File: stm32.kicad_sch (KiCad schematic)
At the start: 13 parts, among them J102 Conn_ARM_JTAG_SWD_10, U101 STM32F302CBTx, Y101 8MHz / 20pF

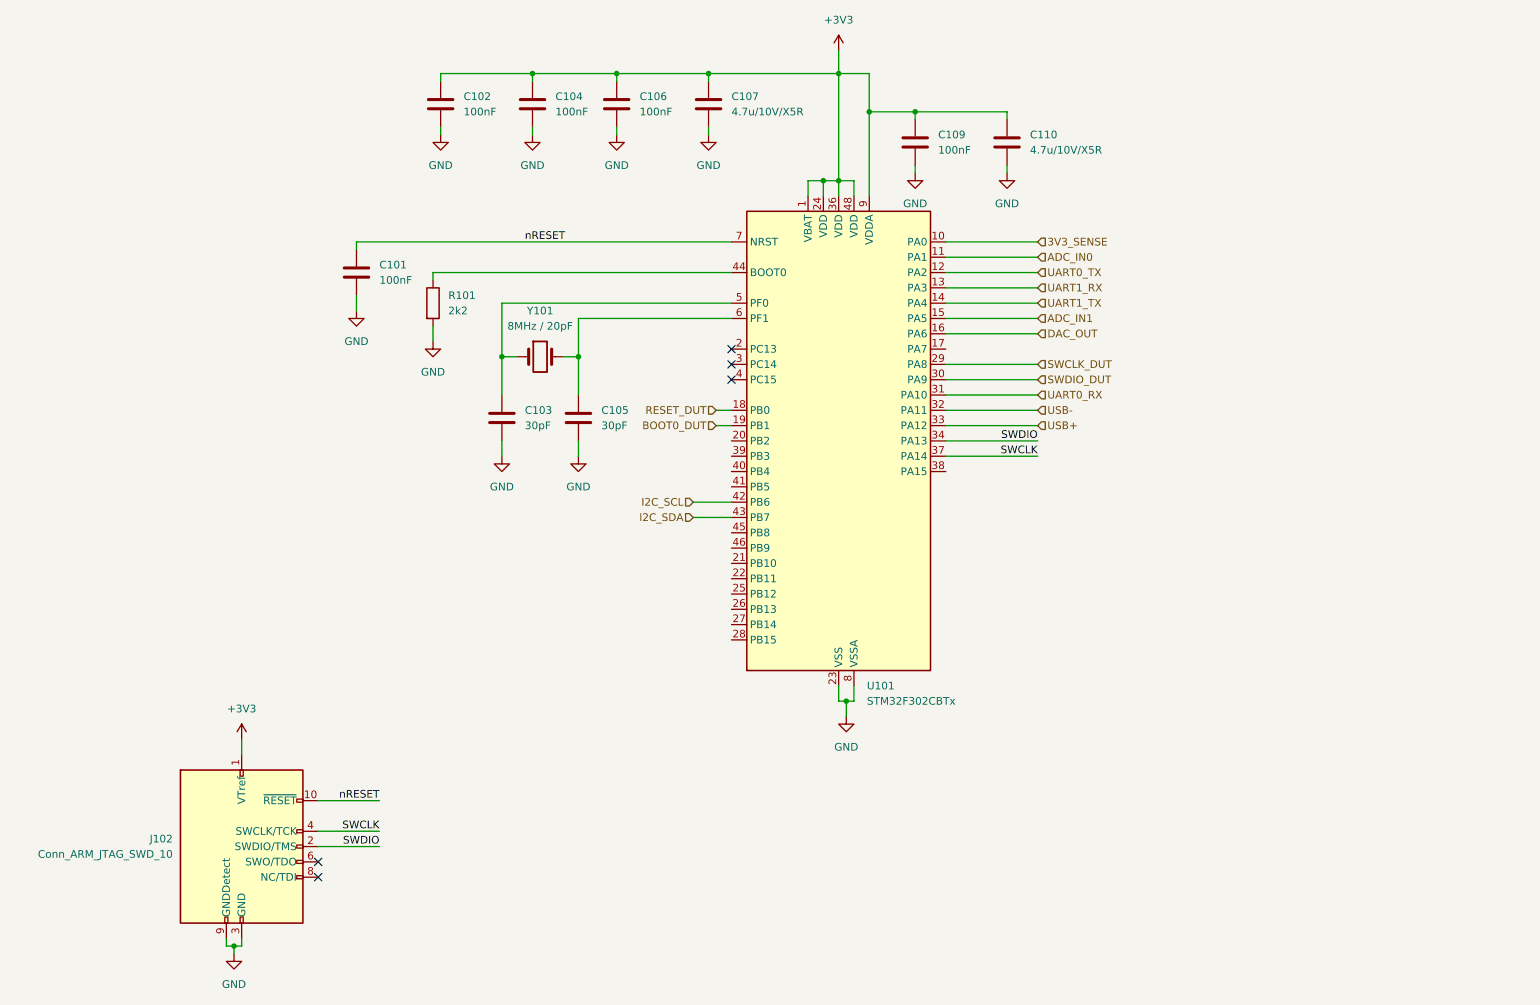
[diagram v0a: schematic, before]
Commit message: add basic structure, update readme
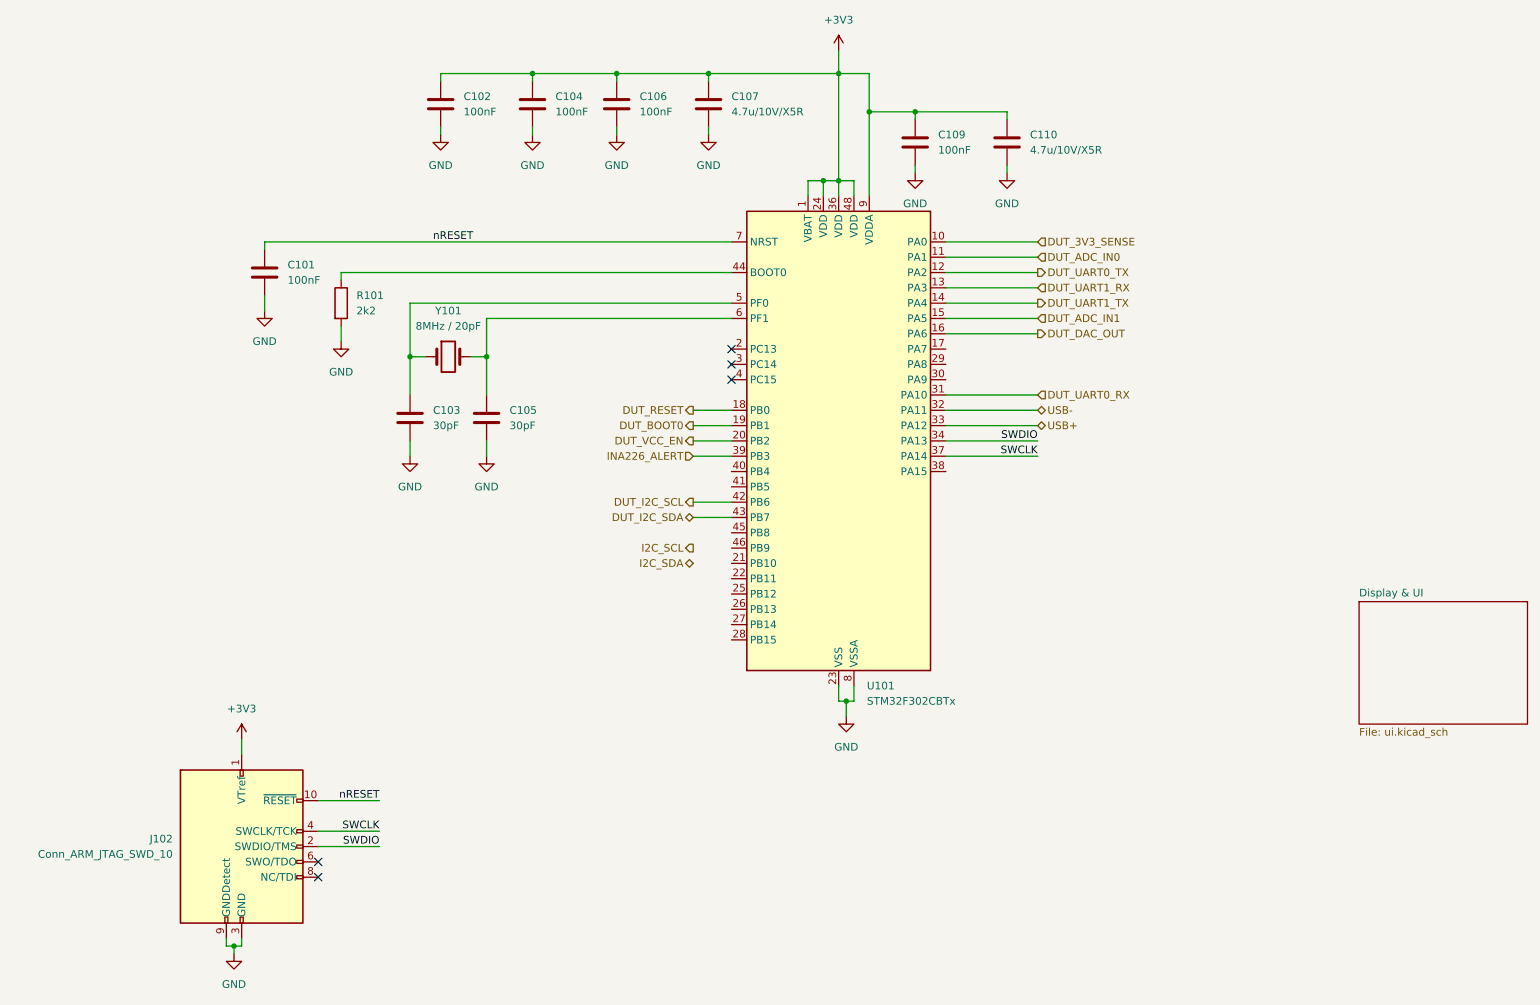
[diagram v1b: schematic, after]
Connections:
- net I2C_SCL: no longer U101.42 (PB6)
- net I2C_SDA: no longer U101.43 (PB7)
- net DUT_VCC_EN: now reaches U101.20 (PB2)
- net INA226_ALERT: now reaches U101.39 (PB3)
- net 3V3_SENSE renamed DUT_3V3_SENSE
- net ADC_IN0 renamed DUT_ADC_IN0
- net ADC_IN1 renamed DUT_ADC_IN1
- net BOOT0_DUT renamed DUT_BOOT0
- net DAC_OUT renamed DUT_DAC_OUT
- net RESET_DUT renamed DUT_RESET
- net SWCLK_DUT: no longer names the net of U101.29 (PA8)
- net SWDIO_DUT: no longer names the net of U101.30 (PA9)
- net UART0_RX renamed DUT_UART0_RX
- net UART0_TX renamed DUT_UART0_TX
- net UART1_RX renamed DUT_UART1_RX
- net UART1_TX renamed DUT_UART1_TX
- new net DUT_I2C_SCL: U101.42 (PB6)
- new net DUT_I2C_SDA: U101.43 (PB7)
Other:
- added sheet Display & UI (ui.kicad_sch)
- moved on the sheet: C101, C103, C105, R101, Y101

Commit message: Update schematic for DebugBoard with connector and power symbols.
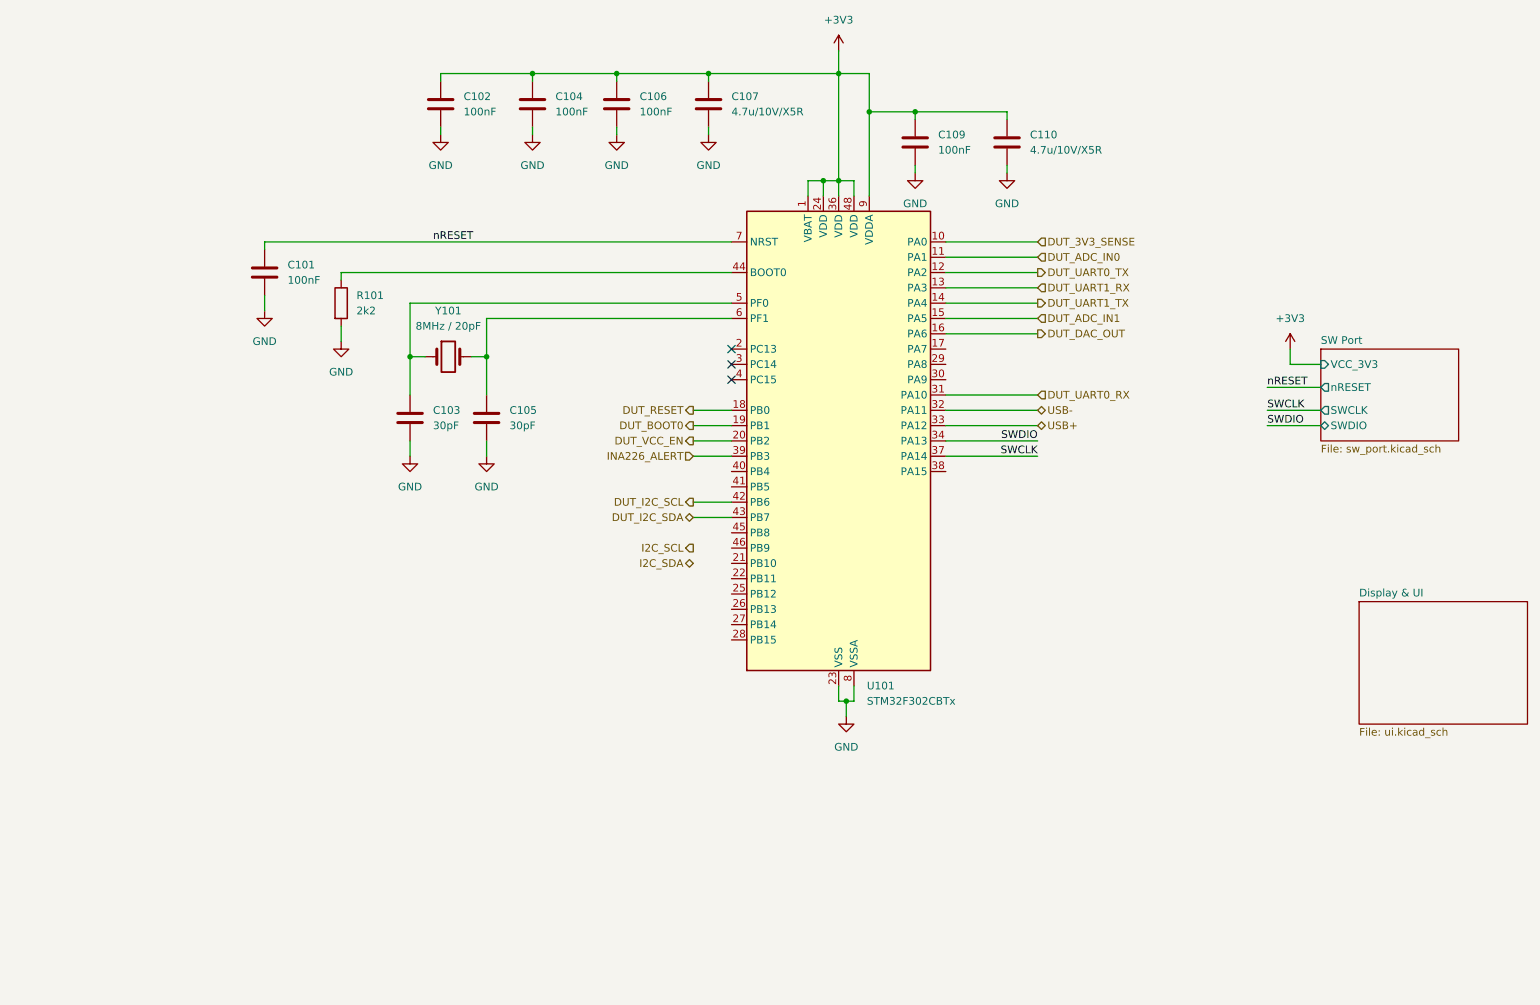
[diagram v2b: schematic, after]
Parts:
- removed J102: Conn_ARM_JTAG_SWD_10, Connector_PinHeader_2.54mm:PinHeader_2x05_P2.54mm_Horizontal, symbol Connector:Conn_ARM_JTAG_SWD_10
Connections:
- no-connect marks 5 -> 3
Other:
- added sheet SW Port (sw_port.kicad_sch)

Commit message: Update USB-C and USB-Hub Schematics with New Titles and Reference Changes
- Changed title from "DebugBoard" to "USB-C" in usb_c.kicad_sch.
- Changed title from "DebugBoard" to "USB-Hub" in usb_hub.kicad_sch.
- Updated multiple component references in usb_c.kicad_sch to new identifiers (#PWR0301 to #PWR0312, D301, U301, etc.).
- Updated component reference from "R103" to "R501" in usb_hub.kicad_sch.
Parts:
- renumbered C101 to C201, C103 to C202, C102 to C203, C105 to C204, C104 to C205, C106 to C206, C107 to C207, C109 to C208, C110 to C209, R101 to R201, U101 to U201, Y101 to Y201
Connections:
- net DUT_RESET renamed DUT_nRESET
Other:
- sheet Display & UI ports: added BUTTON_DOWN, BUTTON_OK, BUTTON_UP, I2C_SCL, I2C_SDA; removed none
- title: DebugBoard -> Debug-Controller

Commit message: Refactor code structure for improved readability and maintainability
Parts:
- added R202, R203, R204, R205: 4k7, Resistor_SMD:R_0805_2012Metric, symbol Device:R
- added R206, R207: 100k, Resistor_SMD:R_0805_2012Metric, symbol Device:R
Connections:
- net +3V3: now also R202.1, R203.1, R204.1, R205.1
- net BUTTON_DOWN: now also U201.28 (PB15)
- net BUTTON_OK: now also U201.27 (PB14)
- net BUTTON_UP: now also U201.26 (PB13)
- net DUT_3V3_SENSE: now also R207.1; no longer U201.10 (PA0)
- net DUT_I2C_SCL: now also R202.2
- net DUT_I2C_SDA: now also R203.2
- net GND: now also R206.2
- net I2C_SCL: now also U201.45 (PB8), R204.2
- net I2C_SDA: now also U201.46 (PB9), R205.2
- new net DUT_3V3_SENSE_DIV: R206.1, R207.2, U201.10 (PA0)
- no-connect marks 3 -> 12

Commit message: update pcb
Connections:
- net BUTTON_DOWN: now also U201.26 (PB13); no longer U201.28 (PB15)
- net BUTTON_UP: now also U201.28 (PB15); no longer U201.26 (PB13)
- net DUT_BOOT0: now also U201.18 (PB0); no longer U201.19 (PB1)
- net DUT_DAC_OUT: now also U201.14 (PA4); no longer U201.16 (PA6)
- net DUT_UART0_RX: now also U201.40 (PB4); no longer U201.31 (PA10)
- net DUT_UART0_TX: now also U201.39 (PB3); no longer U201.12 (PA2)
- net DUT_UART1_RX: now also U201.22 (PB11); no longer U201.13 (PA3)
- net DUT_UART1_TX: now also U201.21 (PB10); no longer U201.14 (PA4)
- net DUT_VCC_EN: now also U201.2 (PC13); no longer U201.20 (PB2)
- net DUT_nRESET: now also U201.17 (PA7); no longer U201.18 (PB0)
- net I2C_SCL: now also U201.30 (PA9); no longer U201.45 (PB8)
- net I2C_SDA: now also U201.31 (PA10); no longer U201.46 (PB9)
- net INA226_ALERT: now also U201.3 (PC14); no longer U201.39 (PB3)
